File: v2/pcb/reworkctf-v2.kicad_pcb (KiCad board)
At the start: 4 copper layers, 54 x 50 mm, 131 parts, among them J1 USB_C_Receptacle_USB2.0, J10 TESTPOINT, J11 TESTPOINT, J12 TESTPOINT, J13 TESTPOINT, J14 TESTPOINT, J15 TESTPOINT, J16 TESTPOINT, J17 TESTPOINT, J2 CORTEX_DEBUG_ETM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

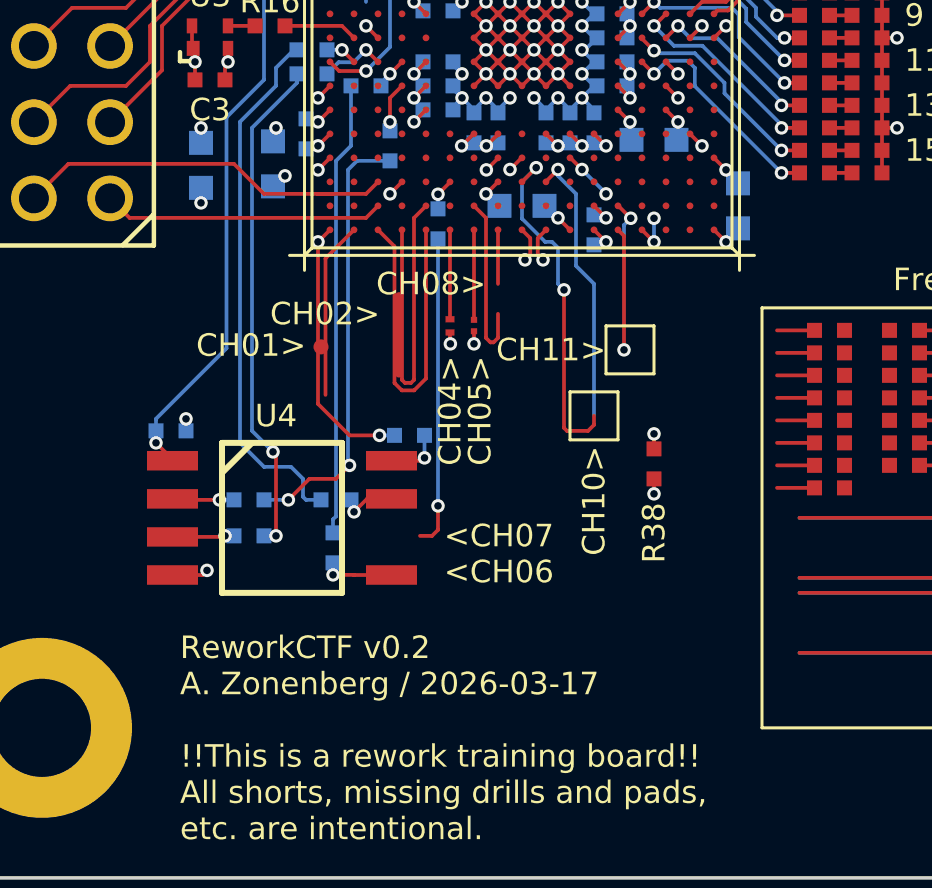
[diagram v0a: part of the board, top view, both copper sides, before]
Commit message: Added strap via to wrong net. Should be ready to order, I think
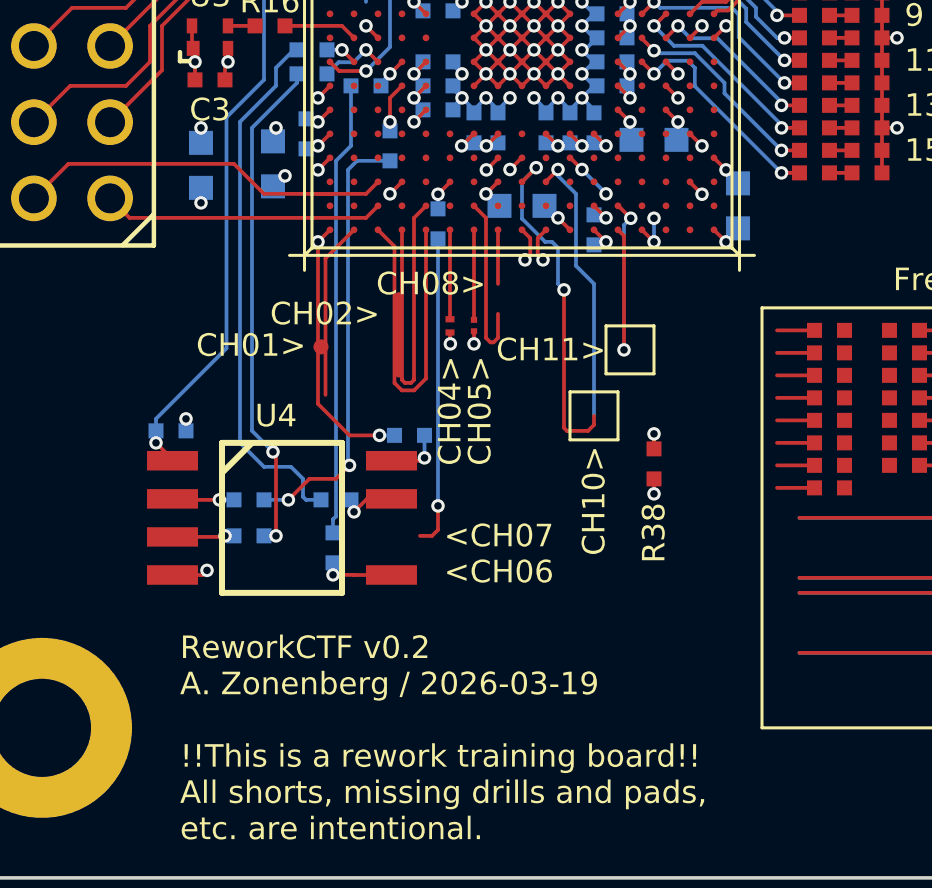
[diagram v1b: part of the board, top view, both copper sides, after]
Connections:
- U1 pad R16: unconnected-(U1D-PD12-PadR16) -> /GND
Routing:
- net /GND: track 352.9 -> 354.1 mm, vias 84 -> 85
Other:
- board text added: "CH16>"
- board text added: "ReworkCTF v0.2 A. Zonenberg / 2026-03-19 !!This is a rework training board!! All shorts, missing drills and pads, etc. are intentional."
- board text removed: "ReworkCTF v0.2 A. Zonenberg / 2026-03-17 !!This is a rework training board!! All shorts, missing drills and pads, etc. are intentional."
